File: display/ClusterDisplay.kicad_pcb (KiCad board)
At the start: 4 copper layers, 364.8 x 124 mm, 76 parts, among them J1 Verdin iMX95, J10 RTC coin cell, J2 Power in, J3 CAN to ECU, J4 DM-TFTR50-413 panel, J8 JTAG debug, J9 Buttons, Q1 NFET diode, Q2 NFET pass, Q3 MFT6N2A5S23A (AEC-Q101, 60V/2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, U1 LM74930-Q1, U2 LM61460-Q1, U3 TLV767-Q1, U4 TCAN1044V-Q1, U6 TPS60403-Q1, U7 AL8853AQ

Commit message: Shrink display/ from 364.8x124.0 to 180.8x163.9mm; add the real tach-face art
User asked directly: "does the SOMM board need to be so large?" - no,
it didn't. Two real, separate causes, both fixed:

1. The board's WIDTH was actually driven by laying all 5 circuit zones
   out in a single left-to-right row (summing to ~359mm) - a layout
   choice copied from gauges/'s own CORE_ZONES arrangement without
   reconsidering that gauges/'s single row exists because of a real
   external constraint (4 aux-gauge connectors reaching real, fixed
   dash holes) that doesn't apply to this board at all. Added
   pack_sized_blocks() - the same real skyline algorithm, generalized
   to pack pre-sized rectangles instead of footprints - and used it to
   arrange the 5 zones into a real 2D grid (2 rows) instead of one long
   row.

2. The module keepout (90x90mm) was more conservative than the real
   geometry justifies. Pulled the SODIMM-260 socket's own real
   courtyard directly from its footprint (27.1 x 79.0mm, an irregular
   shape with an angled ejector-latch cutout) - the module's 69.6mm
   length already lines up with the courtyard's 79.0mm long axis, so
   only ONE axis needs real margin for the module's unconfirmed
   overhang direction, not both simultaneously. Retargeted to a real
   60x82mm keepout.

Net real result: 180.8 x 163.9mm, down from 364.8 x 124.0mm (total
area -35%). BOARD_MARGIN bumped 3.0->12.0mm - a real corner collision
between U4 and a mounting hole surfaced once the board got this much
tighter, same category of bug the original board's own mounting-hole
work already hit once (naive margins vs real content need real
verification, not assumption).

Also added the real back-silkscreen art gauges/ already carries (tach
face + CLUSTER wordmark, inherited from the original single-board
design) - display/ had none yet. Re-derived the layout for this
board's square proportions (gauge centered, wordmark stacked below)
rather than copying gauges/'s wide-strip side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
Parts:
- moved C39 171.1 mm to (204.5, 169.3)
- moved J8 171.1 mm to (168.3, 170.3)
- moved R45 171.1 mm to (214.4, 169.3)
- moved R47 171.1 mm to (204.5, 172.8)
- moved R49 171.1 mm to (214.4, 172.8)
- moved J10 171.1 mm to (148.1, 178.6)
- moved J9 171.1 mm to (191.6, 170.3)
- moved R44 171.1 mm to (209.4, 169.3)
- moved R46 171.1 mm to (218.6, 170.0)
- moved R48 171.1 mm to (209.4, 172.8)
- moved C1 101.4 mm to (195.9, 197.3)
- moved C4 101.4 mm to (210.7, 197.3)
- moved C6 101.4 mm to (195.9, 200.8)
- moved R1 101.4 mm to (210.7, 200.8)
- moved R11 101.4 mm to (170.6, 204.1)
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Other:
- board size 364.8 x 124 mm -> 180.8 x 163.9 mm
- board text added: "0"
- board text added: "1"
- board text added: "2"
- board text added: "3"
- board text added: "4"
- board text added: "5"
- board text added: "6"
- board text added: "7"
- board text added: "8"
- board text added: "ANDROID DISPLAY CARRIER"
- board text added: "CLUSTER"
- board text added: "JESSIE'S CARS"
- board text added: "x1000 RPM"

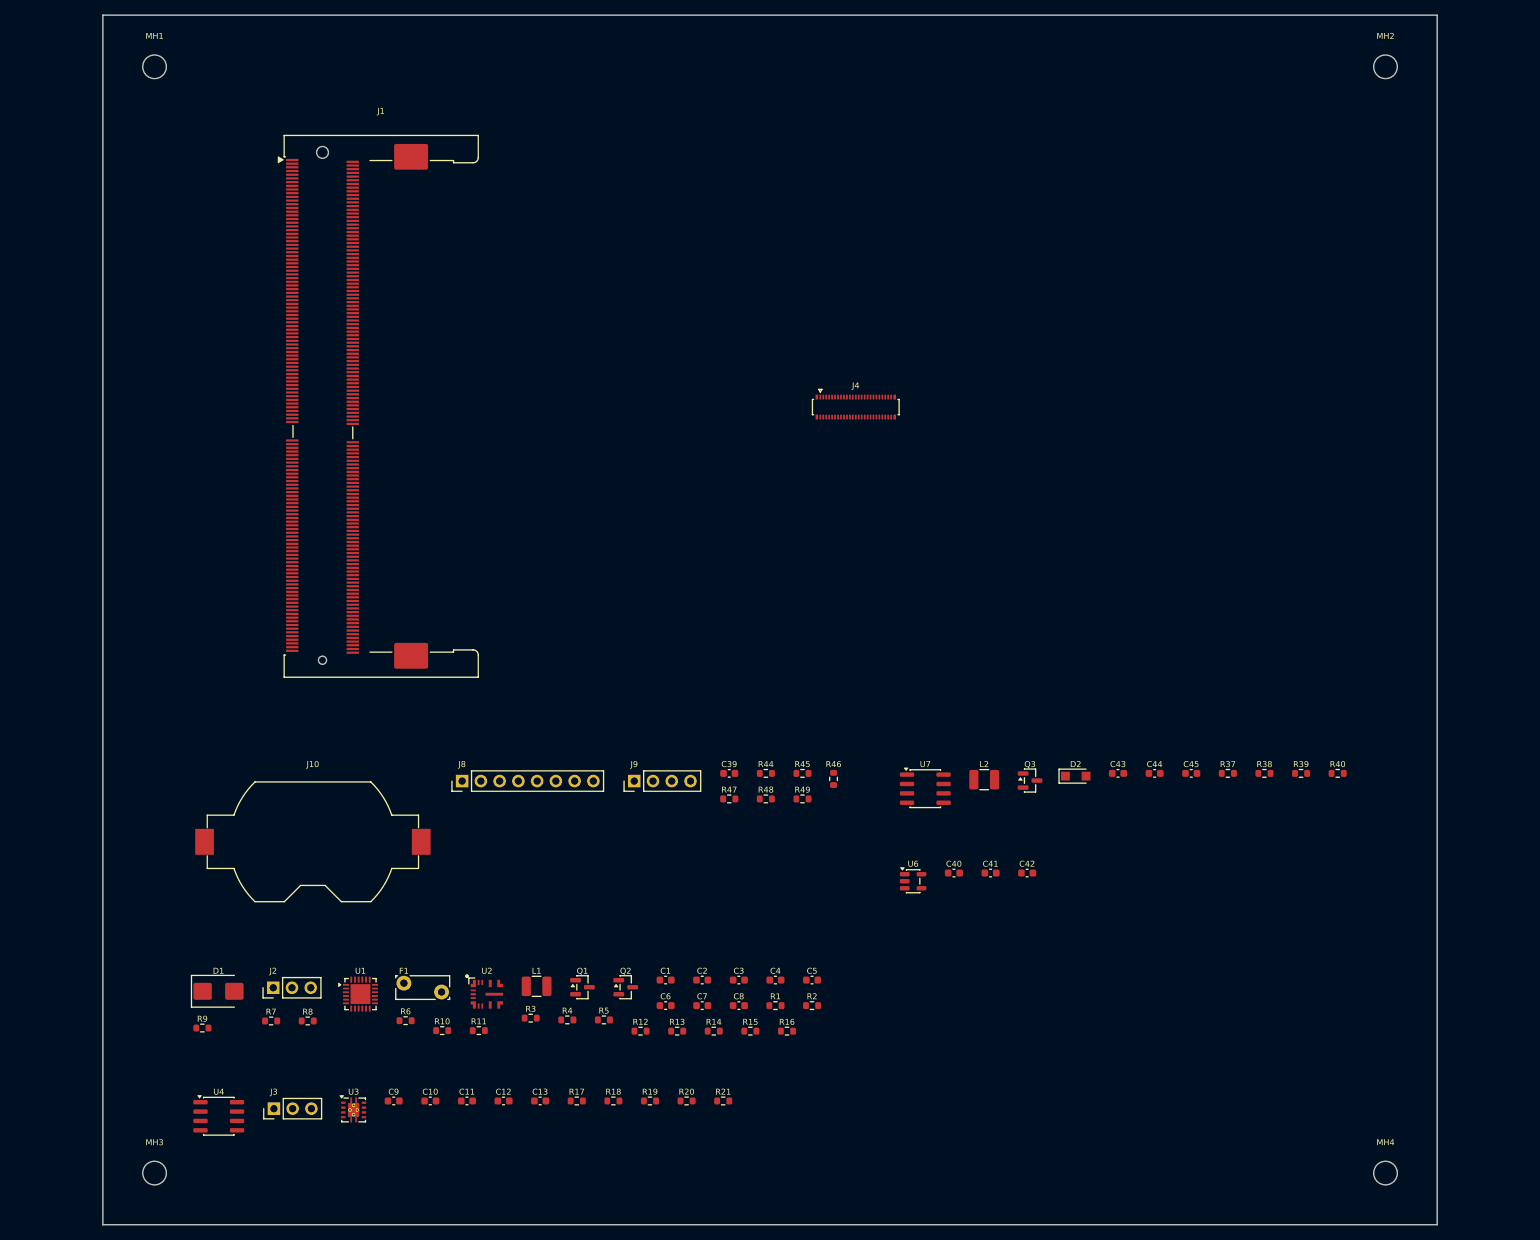
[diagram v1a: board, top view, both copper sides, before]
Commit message: display: unify layout pack around module keepout, redesign back art placement
Replace the top-band/zone-band split with a single 2D pack: the Verdin
module keepout is a real fixed obstacle (seeded skyline), and J4 plus
all 5 circuit zones are packed into the space actually left around it.
Board shrinks from 180.8x163.9mm to a more honest 204.5x114mm with no
leftover strip beside J4.

Back-silkscreen tach face + wordmark placement is redone too: a first
side-by-side layout (copied from gauges/) put the gauge right where
J1's real SODIMM alignment pegs are, since the previous safe-area math
conflated front-side zone content with the actual back-side constraint
(real thru-hole pads only - NPTH pegs don't trip silk_over_copper, so
this wasn't caught by DRC). Now the code computes every real thru-hole
pad's box, finds the actual widest clear vertical corridor, and stacks
the gauge above the wordmark inside it - verified against real pad
geometry instead of an assumed rectangle.

Co-Authored-By: Claude Sonnet 5 <noreply@anthropic.com>
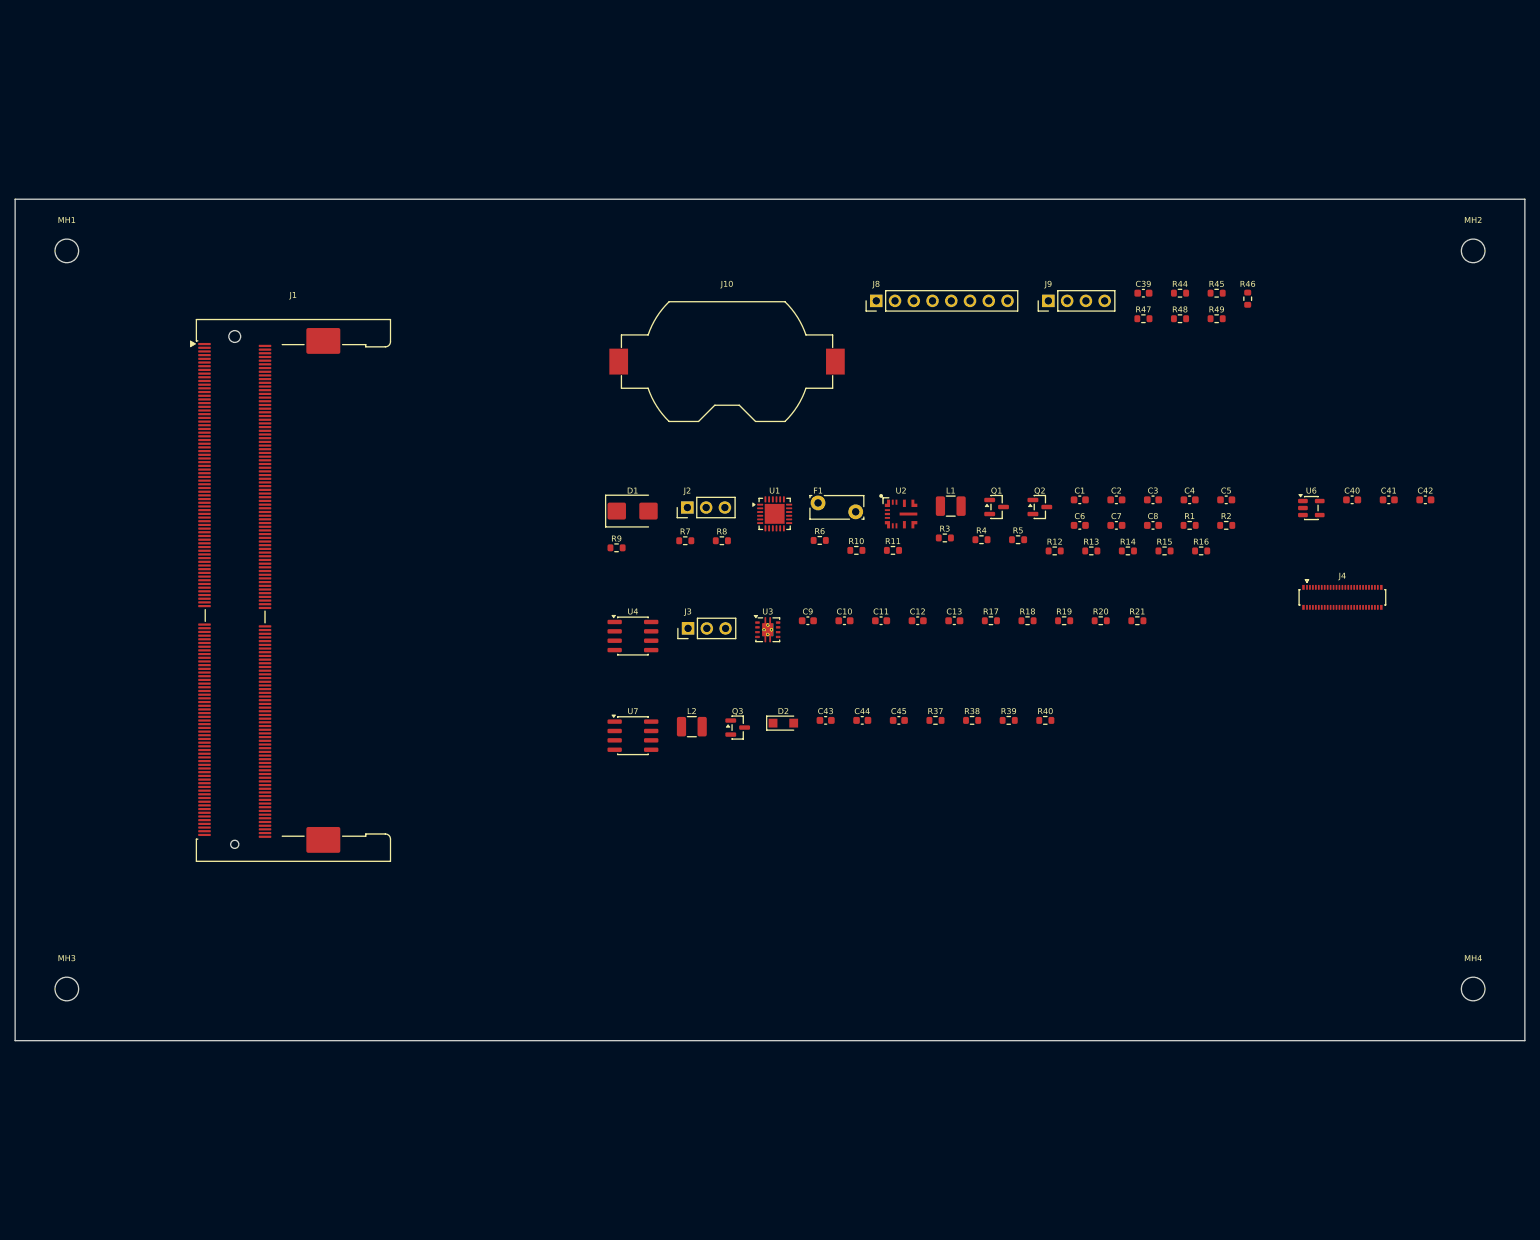
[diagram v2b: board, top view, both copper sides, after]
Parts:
- moved J8 85.9 mm to (224.4, 105.3)
- moved C2 85.9 mm to (256.9, 132.2)
- moved C4 85.9 mm to (266.9, 132.2)
- moved C5 85.9 mm to (271.8, 132.2)
- moved C7 85.9 mm to (256.9, 135.7)
- moved J10 85.9 mm to (204.2, 113.5)
- moved J2 85.9 mm to (198.8, 133.3)
- moved J3 85.9 mm to (198.9, 149.7)
- moved Q2 85.9 mm to (246.6, 133.2)
- moved R1 85.9 mm to (266.9, 135.7)
- moved R13 85.9 mm to (253.5, 139.2)
- moved R14 85.9 mm to (258.5, 139.2)
- moved R16 85.9 mm to (268.4, 139.2)
- moved R2 85.9 mm to (271.8, 135.7)
- moved R4 85.9 mm to (238.7, 137.6)
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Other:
- board size 180.8 x 163.9 mm -> 204.5 x 114 mm

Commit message: display: replace bin-packed layout with a deliberate 2-column grid
The previous unified pack read as algorithmically arranged, not
designed: the block-packer let J4 (the panel connector) land wherever
was tightest among the 5 zones, disconnected from any neighbor, and
each zone started at its own independent X with no shared alignment.
Zones also mixed part orientations internally whenever a 90-degree
rotation packed slightly tighter.

Replace both. J4 now anchors the top of a real right-hand column; the
5 zones fill in below it across 2 height-balanced columns, in their
own functional order (not resorted by size), each row left-aligned to
its column - a real grid, not a bin-pack. skyline_pack() gained an
allow_rotate flag, disabled for zone packing, so each zone reads as one
consistently-oriented row instead of a tightest-fit jumble.

pack_sized_blocks() is now dead code (nothing calls the free-for-all
block packer anymore) - removed rather than left unused.

Board grew 204.5x114.0mm -> 253.9x114.0mm, the real cost of alignment
over minimum area. DRC-clean.

Co-Authored-By: Claude Sonnet 5 <noreply@anthropic.com>
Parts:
- moved J4 124.7 mm to (169.3, 105.9)
- moved C40 118.2 mm to (170.6, 133.4)
- moved C42 118.2 mm to (180.6, 133.4)
- moved C41 118.2 mm to (175.6, 133.4)
- moved U6 118.2 mm to (165.1, 134.6)
- moved J3 75.8 mm to (267.7, 117.9), turned to 0 degrees
- moved U4 75.8 mm to (260.2, 118.9)
- moved C43 74.5 mm to (286.3, 133.4)
- moved C45 74.5 mm to (296.2, 133.4)
- moved L2 74.5 mm to (268.2, 134.3)
- moved R37 74.5 mm to (301.2, 133.4)
- moved R39 74.5 mm to (311.1, 133.4)
- moved C44 74.5 mm to (291.3, 133.4)
- moved D2 74.5 mm to (280.6, 133.8)
- moved Q3 74.5 mm to (274.4, 134.4)
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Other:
- board size 204.5 x 114 mm -> 253.9 x 114 mm

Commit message: display: undo the rigid column grid, fold J4 into CONTROL, tight-pack zones
Direct user correction after the 2-column grid: "look at all the dead
space. parts do not need to be in line." The grid fixed the floating-
connector complaint by forcing every zone into aligned columns, but
columns of very different real heights (module-anchored column A vs.
J4-only column B) left two large dead rectangles - trading one problem
for a worse one.

Revert to a tight bin-pack for arranging zones around the module
keepout (pack_sized_blocks restored), but keep the real fix for J4:
instead of pulling it out as its own reserved block (which is what let
it land disconnected from everything in the very first unified-pack
version), it's now part of CORE_ZONES' own CONTROL list, alongside the
other external connectors (J8/J9/J10) it actually belongs with. Board:
253.9x114.0mm -> 229.5x114.0mm, DRC-clean, no forced alignment and no
large dead voids.

Co-Authored-By: Claude Sonnet 5 <noreply@anthropic.com>
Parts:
- moved C41 93.6 mm to (264.2, 163.7)
- moved C40 93.6 mm to (259.3, 163.7)
- moved C42 93.6 mm to (269.2, 163.7)
- moved U6 93.6 mm to (253.7, 164.8)
- moved C13 87.8 mm to (217.4, 150.2)
- moved J3 87.8 mm to (186.4, 151.2)
- moved R19 87.8 mm to (232.3, 150.2)
- moved C11 87.8 mm to (207.5, 150.2)
- moved C12 87.8 mm to (212.4, 150.2)
- moved C9 87.8 mm to (197.6, 150.2)
- moved R17 87.8 mm to (222.4, 150.2)
- moved R20 87.8 mm to (237.2, 150.2)
- moved U3 87.8 mm to (192.1, 151.4)
- moved U4 87.8 mm to (178.9, 152.2)
- moved C10 87.8 mm to (202.5, 150.2)
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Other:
- board size 253.9 x 114 mm -> 229.5 x 114 mm
